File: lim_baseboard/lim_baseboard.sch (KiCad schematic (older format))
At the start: 37 parts, among them J1 Conn_02x07_Odd_Even, J2 Conn_02x07_Odd_Even, J3 Conn_02x07_Odd_Even, J4 Conn_02x08_Odd_Even, J5 Conn_02x08_Odd_Even, J6 Conn_02x08_Odd_Even, J7 Conn_02x08_Odd_Even

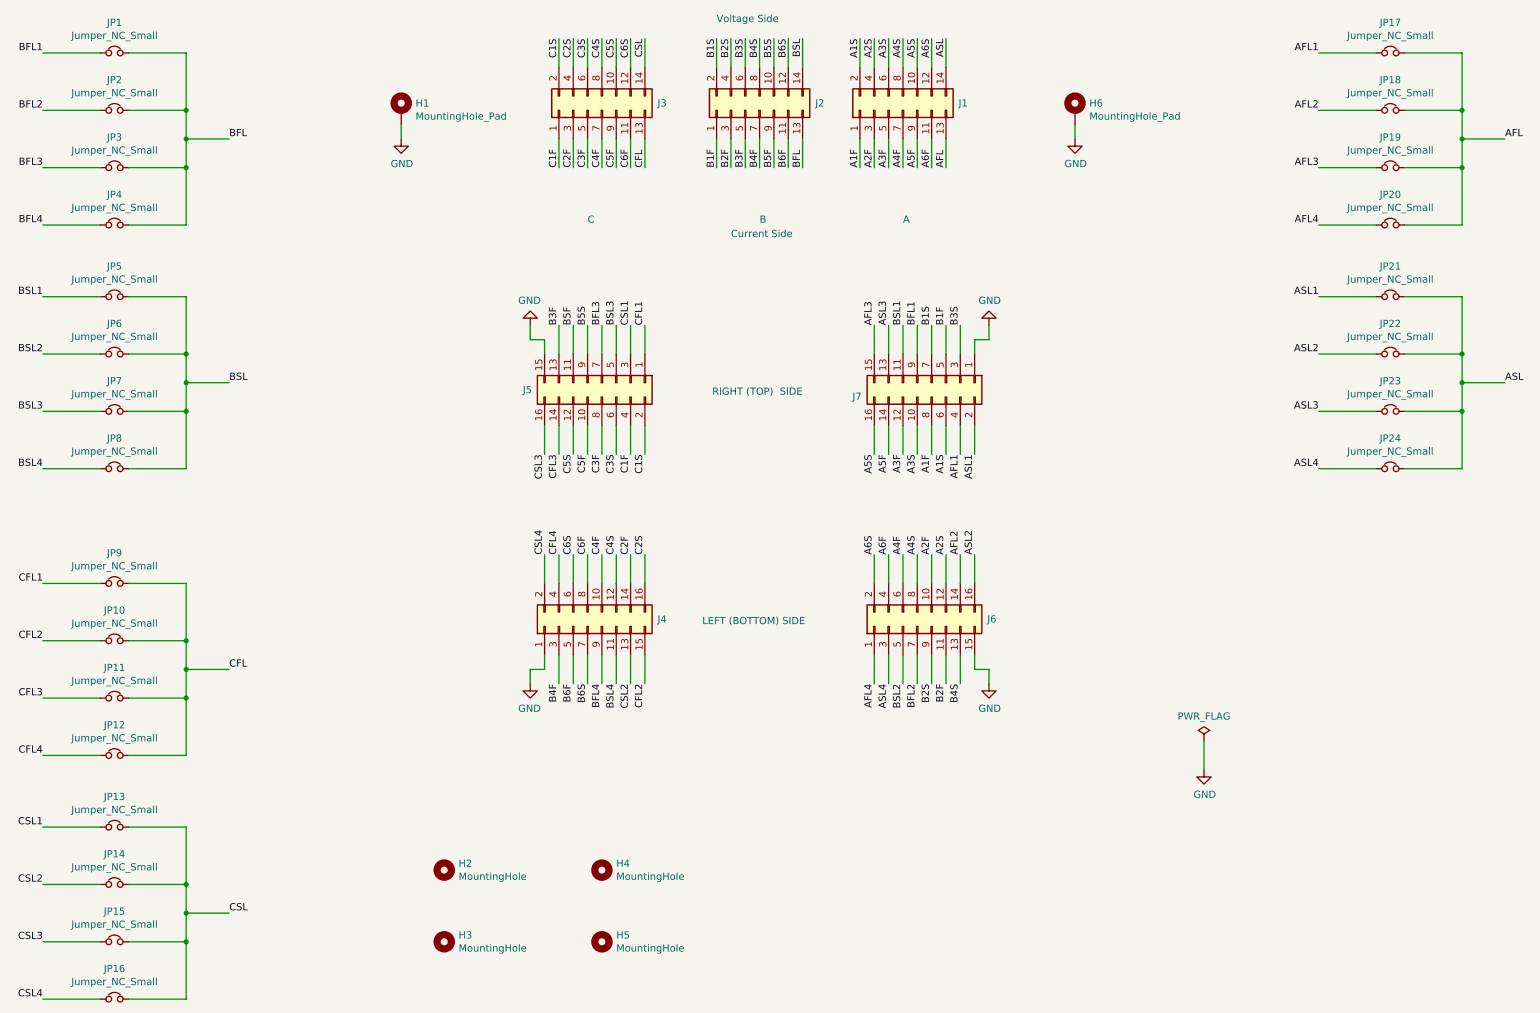
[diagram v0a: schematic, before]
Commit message: fix lim baseboard bug
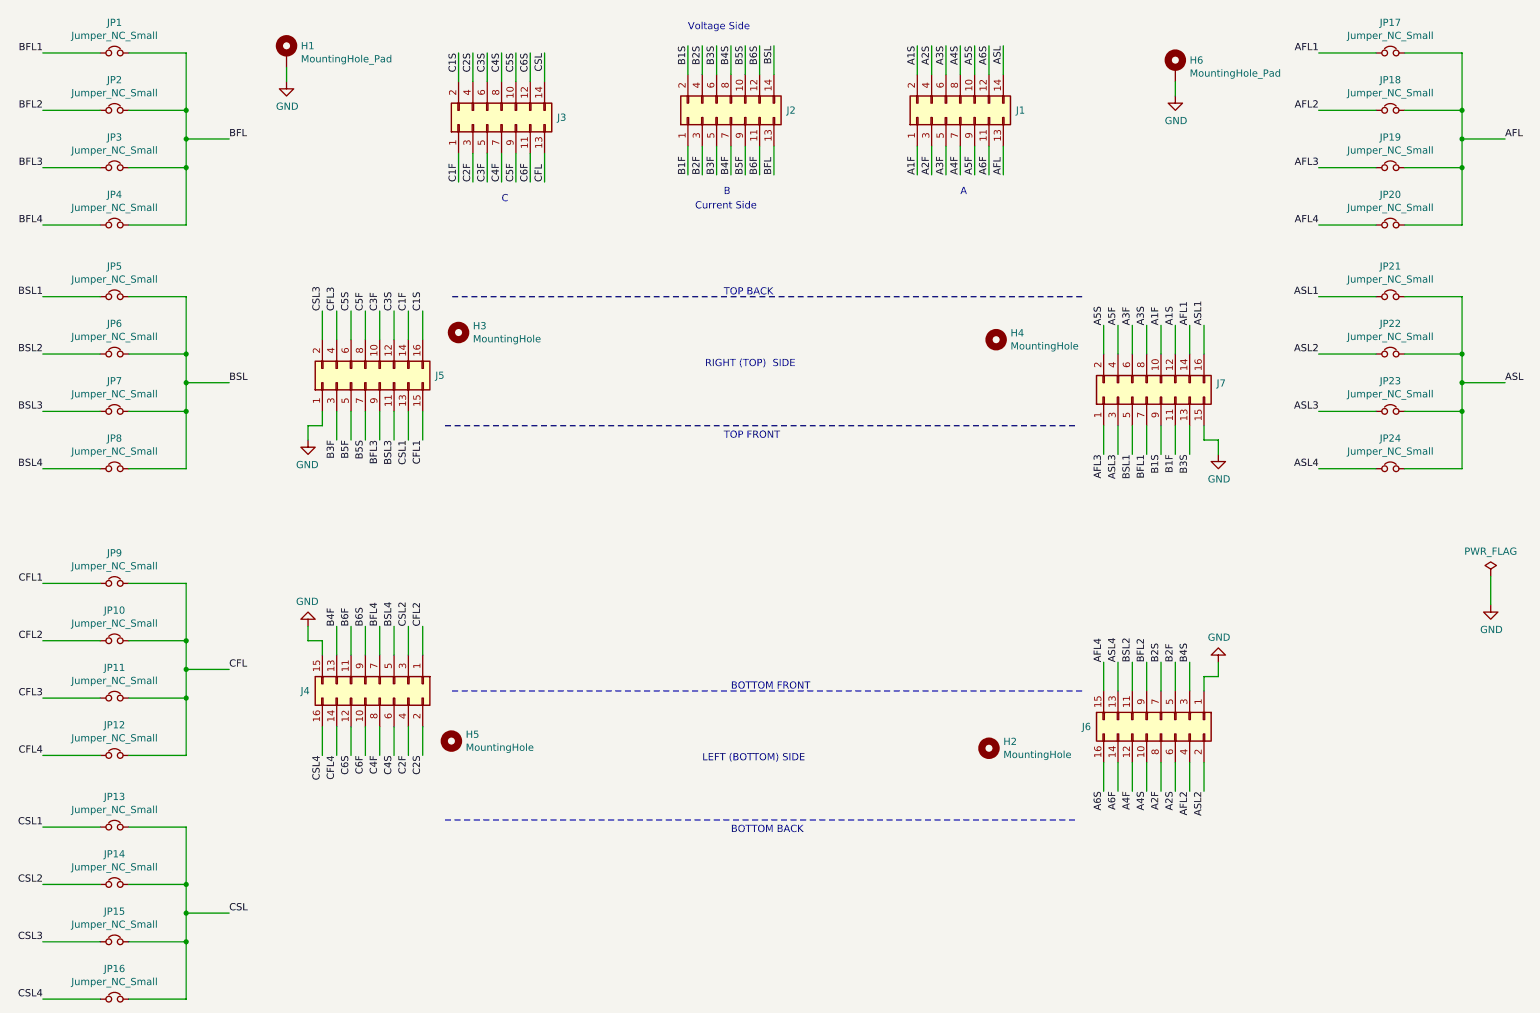
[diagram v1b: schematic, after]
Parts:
- J4, J5, J6, J7: footprint Connector_PCBEdge:Samtec_MECF-08-01-NP-L-DV-WT_2x08_P1.27mm_Socket_Horizontal -> custom:Samtec_MECF-08-01-NP-L-DV-WT_2x08_P1.27mm_Socket_Horizontal_mod
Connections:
- net A1F: now also J7.10 (Pin_10); no longer J7.8 (Pin_8)
- net A1S: now also J7.12 (Pin_12); no longer J7.6 (Pin_6)
- net A2F: now also J6.8 (Pin_8); no longer J6.10 (Pin_10)
- net A2S: now also J6.6 (Pin_6); no longer J6.12 (Pin_12)
- net A3F: now also J7.6 (Pin_6); no longer J7.12 (Pin_12)
- net A3S: now also J7.8 (Pin_8); no longer J7.10 (Pin_10)
- net A4F: now also J6.12 (Pin_12); no longer J6.6 (Pin_6)
- net A4S: now also J6.10 (Pin_10); no longer J6.8 (Pin_8)
- net A5F: now also J7.4 (Pin_4); no longer J7.14 (Pin_14)
- net A5S: now also J7.2 (Pin_2); no longer J7.16 (Pin_16)
- net A6F: now also J6.14 (Pin_14); no longer J6.4 (Pin_4)
- net A6S: now also J6.16 (Pin_16); no longer J6.2 (Pin_2)
- net AFL1: now also J7.14 (Pin_14); no longer J7.4 (Pin_4)
- net AFL2: now also J6.4 (Pin_4); no longer J6.14 (Pin_14)
- net AFL3: now also J7.1 (Pin_1); no longer J7.15 (Pin_15)
- net AFL4: now also J6.15 (Pin_15); no longer J6.1 (Pin_1)
- net ASL1: now also J7.16 (Pin_16); no longer J7.2 (Pin_2)
- net ASL2: now also J6.2 (Pin_2); no longer J6.16 (Pin_16)
- net ASL3: now also J7.3 (Pin_3); no longer J7.13 (Pin_13)
- net ASL4: now also J6.13 (Pin_13); no longer J6.3 (Pin_3)
- net B1F: now also J7.11 (Pin_11); no longer J7.5 (Pin_5)
- net B1S: now also J7.9 (Pin_9); no longer J7.7 (Pin_7)
- net B2F: now also J6.5 (Pin_5); no longer J6.11 (Pin_11)
- net B2S: now also J6.7 (Pin_7); no longer J6.9 (Pin_9)
- net B3F: now also J5.3 (Pin_3); no longer J5.13 (Pin_13)
- net B3S: now also J7.13 (Pin_13); no longer J7.3 (Pin_3)
- net B4F: now also J4.13 (Pin_13); no longer J4.3 (Pin_3)
- net B4S: now also J6.3 (Pin_3); no longer J6.13 (Pin_13)
- net B5F: now also J5.5 (Pin_5); no longer J5.11 (Pin_11)
- net B5S: now also J5.7 (Pin_7); no longer J5.9 (Pin_9)
- net B6F: now also J4.11 (Pin_11); no longer J4.5 (Pin_5)
- net B6S: now also J4.9 (Pin_9); no longer J4.7 (Pin_7)
- net BFL1: now also J7.7 (Pin_7); no longer J7.9 (Pin_9)
- net BFL2: now also J6.9 (Pin_9); no longer J6.7 (Pin_7)
- net BFL3: now also J5.9 (Pin_9); no longer J5.7 (Pin_7)
- net BFL4: now also J4.7 (Pin_7); no longer J4.9 (Pin_9)
- net BSL1: now also J7.5 (Pin_5); no longer J7.11 (Pin_11)
- net BSL2: now also J6.11 (Pin_11); no longer J6.5 (Pin_5)
- net BSL3: now also J5.11 (Pin_11); no longer J5.5 (Pin_5)
- net BSL4: now also J4.5 (Pin_5); no longer J4.11 (Pin_11)
- net C1F: now also J5.14 (Pin_14); no longer J5.4 (Pin_4)
- net C1S: now also J5.16 (Pin_16); no longer J5.2 (Pin_2)
- net C2F: now also J4.4 (Pin_4); no longer J4.14 (Pin_14)
- net C2S: now also J4.2 (Pin_2); no longer J4.16 (Pin_16)
- net C3F: now also J5.10 (Pin_10); no longer J5.8 (Pin_8)
- net C3S: now also J5.12 (Pin_12); no longer J5.6 (Pin_6)
- net C4F: now also J4.8 (Pin_8); no longer J4.10 (Pin_10)
- net C4S: now also J4.6 (Pin_6); no longer J4.12 (Pin_12)
- net C5F: now also J5.8 (Pin_8); no longer J5.10 (Pin_10)
- net C5S: now also J5.6 (Pin_6); no longer J5.12 (Pin_12)
- net C6F: now also J4.10 (Pin_10); no longer J4.8 (Pin_8)
- net C6S: now also J4.12 (Pin_12); no longer J4.6 (Pin_6)
- net CFL1: now also J5.15 (Pin_15); no longer J5.1 (Pin_1)
- net CFL2: now also J4.1 (Pin_1); no longer J4.15 (Pin_15)
- net CFL3: now also J5.4 (Pin_4); no longer J5.14 (Pin_14)
- net CFL4: now also J4.14 (Pin_14); no longer J4.4 (Pin_4)
- net CSL1: now also J5.13 (Pin_13); no longer J5.3 (Pin_3)
- net CSL2: now also J4.3 (Pin_3); no longer J4.13 (Pin_13)
- net CSL3: now also J5.2 (Pin_2); no longer J5.16 (Pin_16)
- net CSL4: now also J4.16 (Pin_16); no longer J4.2 (Pin_2)
- net GND: now also J4.15 (Pin_15), J5.1 (Pin_1), J6.1 (Pin_1), J7.15 (Pin_15); no longer J4.1 (Pin_1), J5.15 (Pin_15), J6.15 (Pin_15), J7.1 (Pin_1)
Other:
- note added: "BOTTOM BACK"
- note added: "BOTTOM FRONT"
- note added: "TOP BACK"
- note added: "TOP FRONT"
- moved on the sheet: H1, H2, H3, H4, H5, H6, J1, J2, J3, J4, J5, J6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
